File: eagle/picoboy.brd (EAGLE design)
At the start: 72 x 121.7 mm, 10 parts, among them U1 RETROESP32_LM4875

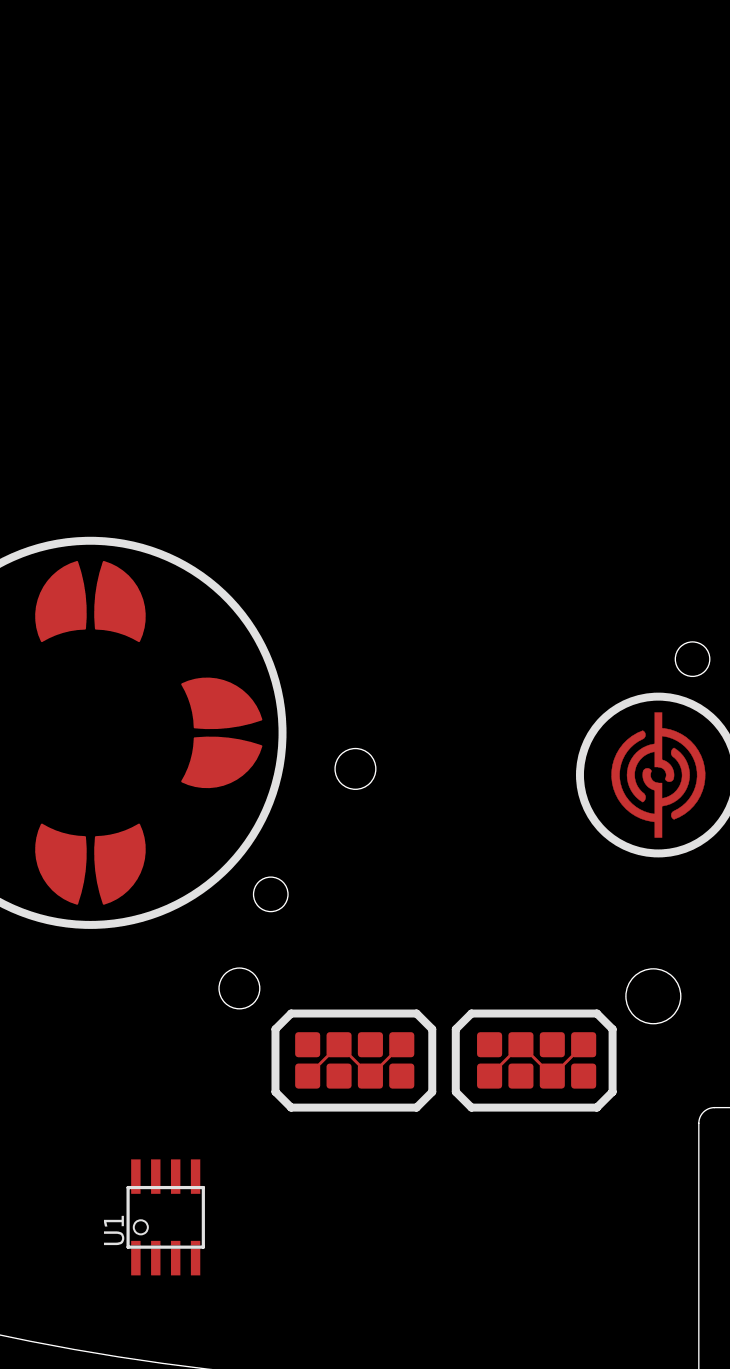
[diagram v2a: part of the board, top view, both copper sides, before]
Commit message: Added devices to library
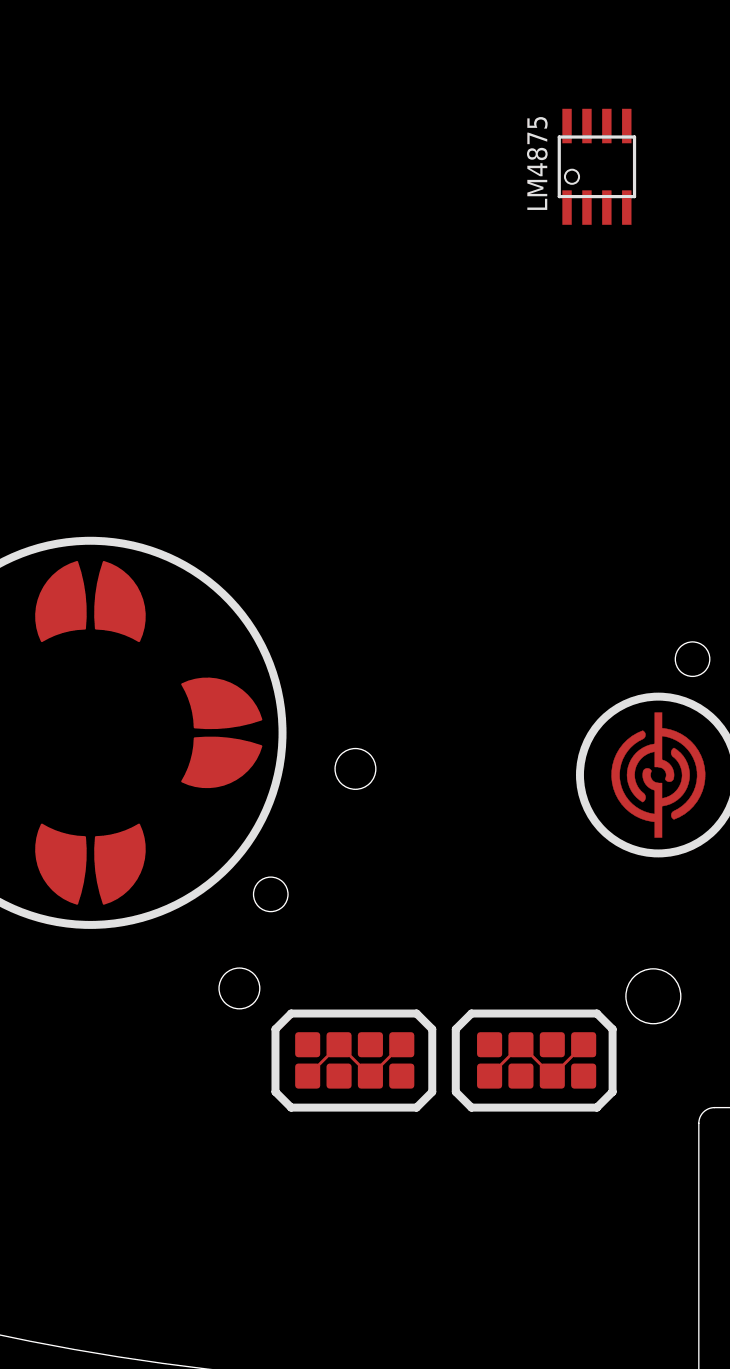
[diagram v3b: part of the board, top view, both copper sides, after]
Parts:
- removed U1: RETROESP32_LM4875, GabozeLite:RETROESP32_SOIC8
- added LM4875: PICOBOY_LM4875, picoboy:PICOBOY_LM4875
- A, B: value RETROESP32_CONDUCTIVE_BUTTONCONDUCTIVE_BUTTON_THICK -> PICOBOY_CONDUCTIVE_BUTTONCONDUCTIVE_BUTTON_THICK; device GabozeLite:RETROESP32_CONDUCTIVE_BUTTON_THICK -> picoboy:PICOBOY_CONDUCTIVE_BUTTON_THICK
- DOWN, LEFT, RIGHT, UP: value RETROESP32_CONDUCTIVE_BUTTONCONDUCTIVE_BUTTON_DIRECTIONAL_THICK -> PICOBOY_CONDUCTIVE_BUTTONCONDUCTIVE_BUTTON_DIRECTIONAL_THICK; device GabozeLite:RETROESP32_CONDUCTIVE_BUTTON_DIRECTIONAL_THICK -> picoboy:PICOBOY_CONDUCTIVE_BUTTON_DIRECTIONAL_THICK
- SELECT, START: value RETROESP32_CONDUCTIVE_BUTTON_STARTSELECTCONDUCTIVE_BUTTON_THICK_STARTSELECT -> PICOBOY_CONDUCTIVE_BUTTON_STARTSELECTCONDUCTIVE_BUTTON_THICK_STARTSELECT; device GabozeLite:RETROESP32_CONDUCTIVE_BUTTON_THICK_STARTSELECT -> picoboy:PICOBOY_CONDUCTIVE_BUTTON_THICK_STARTSELECT
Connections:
- net GND: now also LM4875.6; no longer U1.6
- net VDD: now also LM4875.1; no longer U1.1
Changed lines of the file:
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@@
 </autorouter>
 <elements>
-<element name="UP" library="GabozeLite" package="RETROESP32_CONDUCTIVE_BUTTON_DIRECTIONAL_THICK" value="RETROESP32_CONDUCTIVE_BUTTONCONDUCTIVE_BUTTON_DIRECTIONAL_THICK" x="12.2" y="44.4" smashed="yes" rot="R270"/>
-<element name="RIGHT" library="GabozeLite" package="RETROESP32_CONDUCTIVE_BUTTON_DIRECTIONAL_THICK" value="RETROESP32_CONDUCTIVE_BUTTONCONDUCTIVE_BUTTON_DIRECTIONAL_THICK" x="19.7" y="36.9" smashed="yes" rot="R180"/>
-<element name="DOWN" library="GabozeLite" package="RETROESP32_CONDUCTIVE_BUTTON_DIRECTIONAL_THICK" value="RETROESP32_CONDUCTIVE_BUTTONCONDUCTIVE_BUTTON_DIRECTIONAL_THICK" x="12.2" y="29.4" smashed="yes" rot="R90"/>
-<element name="LEFT" library="GabozeLite" package="RETROESP32_CONDUCTIVE_BUTTON_DIRECTIONAL_THICK" value="RETROESP32_CONDUCTIVE_BUTTONCONDUCTIVE_BUTTON_DIRECTIONAL_THICK" x="4.7" y="36.9" smashed="yes"/>
-<element name="B" library="GabozeLite" package="RETROESP32_CONDUCTIVE_BUTTON_THICK" value="RETROESP32_CONDUCTIVE_BUTTONCONDUCTIVE_BUTTON_THICK" x="48.42" y="34.21" smashed="yes" rot="R180"/>
-<element name="A" library="GabozeLite" package="RETROESP32_CONDUCTIVE_BUTTON_THICK" value="RETROESP32_CONDUCTIVE_BUTTONCONDUCTIVE_BUTTON_THICK" x="62.47" y="38.7" smashed="yes" rot="R180"/>
-<element name="SELECT" library="GabozeLite" package="RETROESP32_CONDUCTIVE_BUTTON_THICK_STARTSELECT" value="RETROESP32_CONDUCTIVE_BUTTON_STARTSELECTCONDUCTIVE_BUTTON_THICK_STARTSELECT" x="29.055" y="16.01" smashed="yes"/>
-<element name="START" library="GabozeLite" package="RETROESP32_CONDUCTIVE_BUTTON_THICK_STARTSELECT" value="RETROESP32_CONDUCTIVE_BUTTON_STARTSELECTCONDUCTIVE_BUTTON_THICK_STARTSELECT" x="40.655" y="16.01" smashed="yes"/>
-<element name="U1" library="GabozeLite" package="RETROESP32_SOIC8" value="RETROESP32_LM4875" x="17" y="6" smashed="yes">
-<attribute name="NAME" x="14.333" y="4.095" size="1.27" layer="25" rot="R90"/>
-<attribute name="VALUE" x="20.937" y="4.095" size="1.27" layer="27" rot="R90"/>
+<element name="UP" library="picoboy" package="PICOBOY_CONDUCTIVE_BUTTON_DIRECTIONAL_THICK" value="PICOBOY_CONDUCTIVE_BUTTONCONDUCTIVE_BUTTON_DIRECTIONAL_THICK" x="12.2" y="44.4" smashed="yes" rot="R270"/>
+<element name="RIGHT" library="picoboy" package="PICOBOY_CONDUCTIVE_BUTTON_DIRECTIONAL_THICK" value="PICOBOY_CONDUCTIVE_BUTTONCONDUCTIVE_BUTTON_DIRECTIONAL_THICK" x="19.7" y="36.9" smashed="yes" rot="R180"/>
+<element name="DOWN" library="picoboy" package="PICOBOY_CONDUCTIVE_BUTTON_DIRECTIONAL_THICK" value="PICOBOY_CONDUCTIVE_BUTTONCONDUCTIVE_BUTTON_DIRECTIONAL_THICK" x="12.2" y="29.4" smashed="yes" rot="R90"/>
+<element name="LEFT" library="picoboy" package="PICOBOY_CONDUCTIVE_BUTTON_DIRECTIONAL_THICK" value="PICOBOY_CONDUCTIVE_BUTTONCONDUCTIVE_BUTTON_DIRECTIONAL_THICK" x="4.7" y="36.9" smashed="yes"/>
+<element name="B" library="picoboy" package="PICOBOY_CONDUCTIVE_BUTTON_THICK" value="PICOBOY_CONDUCTIVE_BUTTONCONDUCTIVE_BUTTON_THICK" x="48.42" y="34.21" smashed="yes" rot="R180"/>
+<element name="A" library="picoboy" package="PICOBOY_CONDUCTIVE_BUTTON_THICK" value="PICOBOY_CONDUCTIVE_BUTTONCONDUCTIVE_BUTTON_THICK" x="62.47" y="38.7" smashed="yes" rot="R180"/>
+<element name="SELECT" library="picoboy" package="PICOBOY_CONDUCTIVE_BUTTON_THICK_STARTSELECT" value="PICOBOY_CONDUCTIVE_BUTTON_STARTSELECTCONDUCTIVE_BUTTON_THICK_STARTSELECT" x="29.055" y="16.01" smashed="yes"/>
+<element name="START" library="picoboy" package="PICOBOY_CONDUCTIVE_BUTTON_THICK_STARTSELECT" value="PICOBOY_CONDUCTIVE_BUTTON_STARTSELECTCONDUCTIVE_BUTTON_THICK_STARTSELECT" x="40.655" y="16.01" smashed="yes"/>
+<element name="LM4875" library="picoboy" package="PICOBOY_LM4875" value="PICOBOY_LM4875" x="44.5" y="73" smashed="yes">
+<attribute name="NAME" x="41.333" y="70.095" size="1.27" layer="25" rot="R90"/>
 </element>
 <element name="U$1" library="picoboy" package="PICOBOY_GBC_BOARD_OUTLINE" value="" x="0" y="0" smashed="yes"/>
@@
 <signals>
 <signal name="GND">
-<contactref element="U1" pad="6"/>
+<contactref element="LM4875" pad="6"/>
 </signal>
 <signal name="VDD">
-<contactref element="U1" pad="1"/>
+<contactref element="LM4875" pad="1"/>
 </signal>
 </signals>

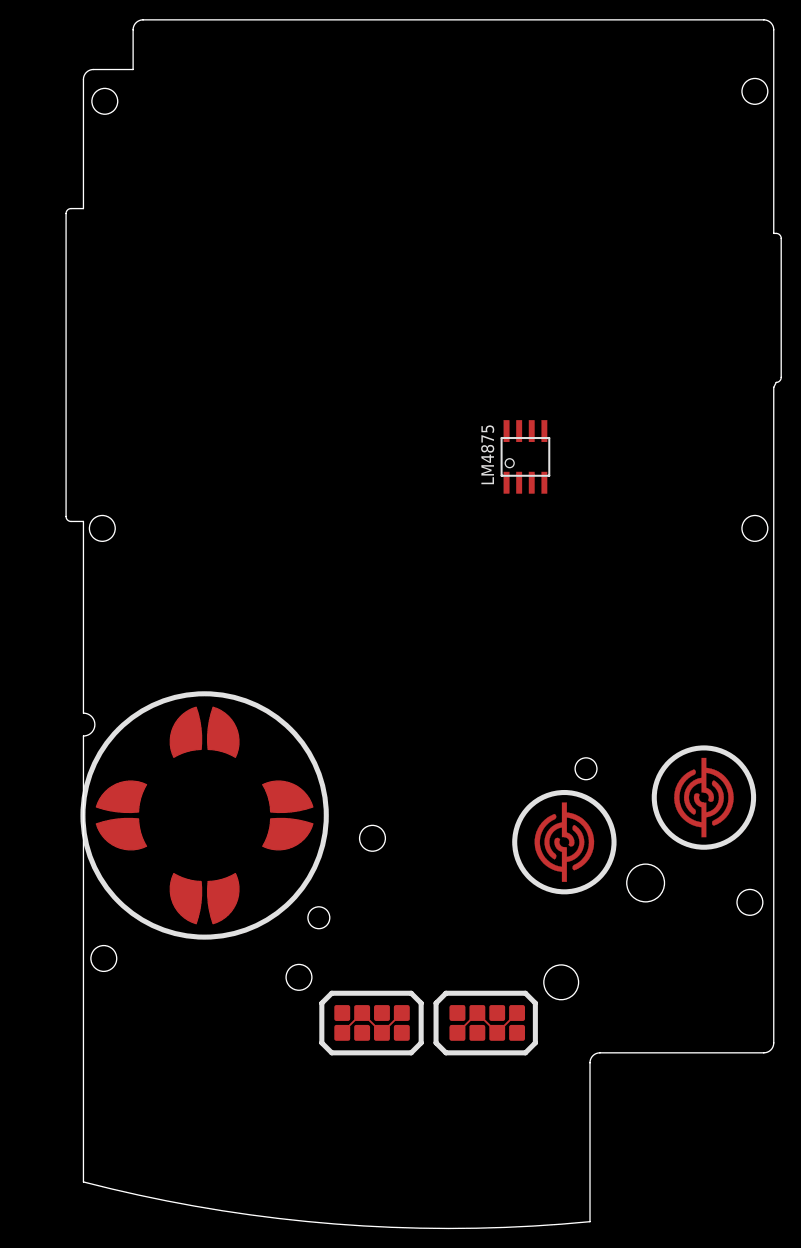
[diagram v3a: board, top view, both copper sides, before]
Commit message: Start amplifier schematics
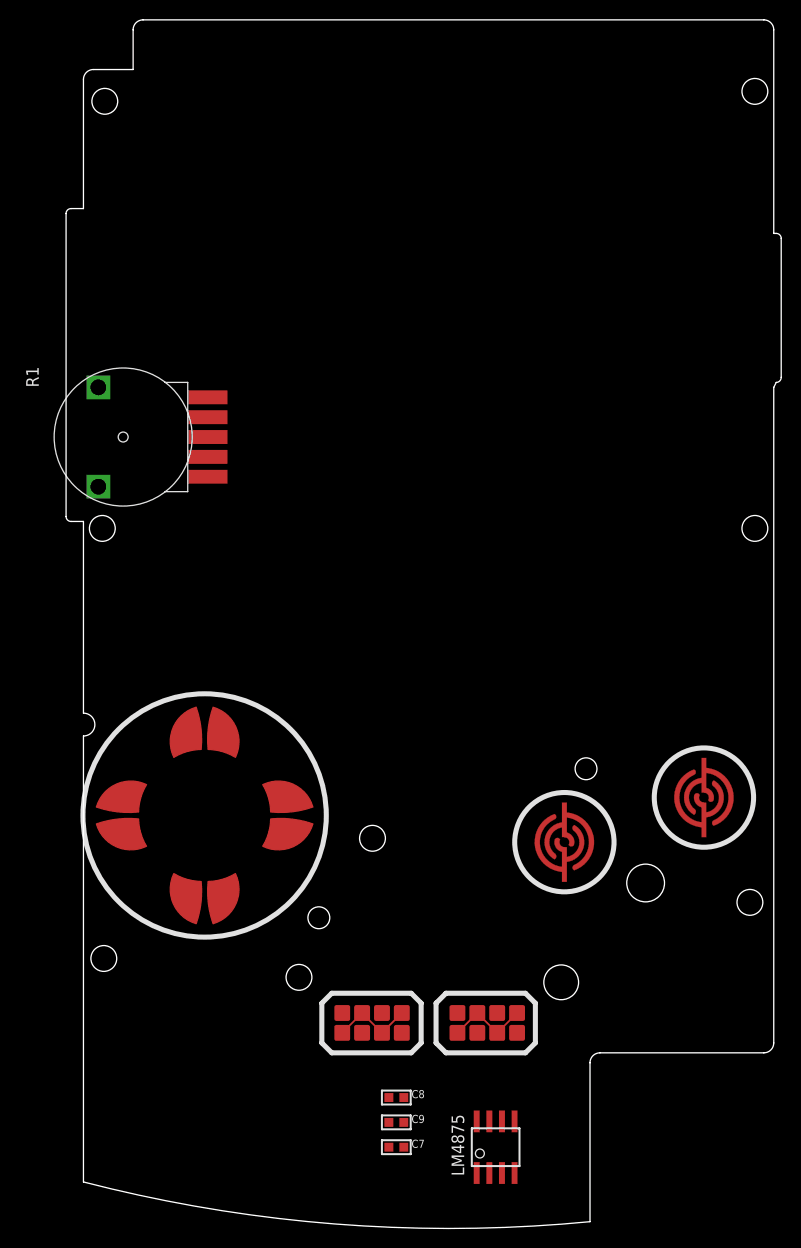
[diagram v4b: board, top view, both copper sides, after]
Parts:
- added C7: 0.22uF, picoboy:PICOBOY_CAPACITOR_0603-MINI
- added C8, C9: 1uF, picoboy:PICOBOY_CAPACITOR_0603-MINI
- added R1: (no value), picoboy:PICOBOY_VOLUME_WHEEL
- moved LM4875 69.6 mm to (41.5, 3.50)
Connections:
- removed net VDD: LM4875.1
- new net 3V3: R1.5
- new net AUDIO: C7.1
- new net N$1: C8.1, LM4875.7
- new net N$2: C9.1, LM4875.1
- new net N$3: C7.2, LM4875.2
- new net N$4: LM4875.4, R1.3
- net GND: now also C8.2, C9.2, R1.1
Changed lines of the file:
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@@
 <element name="SELECT" library="picoboy" package="PICOBOY_CONDUCTIVE_BUTTON_THICK_STARTSELECT" value="PICOBOY_CONDUCTIVE_BUTTON_STARTSELECTCONDUCTIVE_BUTTON_THICK_STARTSELECT" x="29.055" y="16.01" smashed="yes"/>
 <element name="START" library="picoboy" package="PICOBOY_CONDUCTIVE_BUTTON_THICK_STARTSELECT" value="PICOBOY_CONDUCTIVE_BUTTON_STARTSELECTCONDUCTIVE_BUTTON_THICK_STARTSELECT" x="40.655" y="16.01" smashed="yes"/>
-<element name="LM4875" library="picoboy" package="PICOBOY_LM4875" value="PICOBOY_LM4875" x="44.5" y="73" smashed="yes">
-<attribute name="NAME" x="41.333" y="70.095" size="1.27" layer="25" rot="R90"/>
+<element name="LM4875" library="picoboy" package="PICOBOY_LM4875" value="PICOBOY_LM4875" x="41.5" y="3.5" smashed="yes">
+<attribute name="NAME" x="38.333" y="0.595" size="1.27" layer="25" rot="R90"/>
 </element>
 <element name="U$1" library="picoboy" package="PICOBOY_GBC_BOARD_OUTLINE" value="" x="0" y="0" smashed="yes"/>
+<element name="C8" library="picoboy" package="PICOBOY_CAPACITOR_0603-MINI" value="1uF" x="31.5" y="8.5" smashed="yes">
+<attribute name="NAME" x="33.024" y="8.4365" size="0.8128" layer="25" ratio="18"/>
+<attribute name="NAME" x="33.024" y="8.4365" size="0.8128" layer="25" ratio="18"/>
+<attribute name="VALUE" x="33.024" y="7.865" size="0.4064" layer="27" ratio="10"/>
+<attribute name="VALUE" x="33.024" y="7.865" size="0.4064" layer="27" ratio="10"/>
+</element>
+<element name="C9" library="picoboy" package="PICOBOY_CAPACITOR_0603-MINI" value="1uF" x="31.5" y="6" smashed="yes">
+<attribute name="NAME" x="33.024" y="5.9365" size="0.8128" layer="25" ratio="18"/>
+<attribute name="NAME" x="33.024" y="5.9365" size="0.8128" layer="25" ratio="18"/>
+<attribute name="VALUE" x="33.024" y="5.365" size="0.4064" layer="27" ratio="10"/>
+<attribute name="VALUE" x="33.024" y="5.365" size="0.4064" layer="27" ratio="10"/>
+</element>
+<element name="C7" library="picoboy" package="PICOBOY_CAPACITOR_0603-MINI" value="0.22uF" x="31.5" y="3.5" smashed="yes">
+<attribute name="NAME" x="33.024" y="3.4365" size="0.8128" layer="25" ratio="18"/>
+<attribute name="NAME" x="33.024" y="3.4365" size="0.8128" layer="25" ratio="18"/>
+<attribute name="VALUE" x="33.024" y="2.865" size="0.4064" layer="27" ratio="10"/>
+<attribute name="VALUE" x="33.024" y="2.865" size="0.4064" layer="27" ratio="10"/>
+</element>
+<element name="R1" library="picoboy" package="PICOBOY_VOLUME_WHEEL" value="" x="10.5" y="75" smashed="yes" rot="R90">
+<attribute name="NAME" x="-4.5" y="80" size="1.27" layer="25" rot="R90"/>
+<attribute name="VALUE" x="-2.5" y="80" size="1.27" layer="27" rot="R90"/>
+</element>
 </elements>
 <signals>
 <signal name="GND">
 <contactref element="LM4875" pad="6"/>
+<contactref element="C8" pad="2"/>
+<contactref element="C9" pad="2"/>
+<contactref element="R1" pad="1"/>
+<wire x1="32.25" y1="8.5" x2="12.5" y2="71" width="0" layer="19" extent="1-1"/>
+<wire x1="32.25" y1="6" x2="32.25" y2="8.5" width="0" layer="19" extent="1-1"/>
+<wire x1="42.135" y1="6.1" x2="32.25" y2="6" width="0" layer="19" extent="1-1"/>
 </signal>
-<signal name="VDD">
+<signal name="N$1">
+<contactref element="LM4875" pad="7"/>
+<contactref element="C8" pad="1"/>
+<wire x1="30.75" y1="8.5" x2="40.865" y2="6.1" width="0" layer="19" extent="1-1"/>
+</signal>
+<signal name="N$2">
 <contactref element="LM4875" pad="1"/>
+<contactref element="C9" pad="1"/>
+<wire x1="30.75" y1="6" x2="39.595" y2="0.9" width="0" layer="19" extent="1-1"/>
+</signal>
+<signal name="N$3">
+<contactref element="LM4875" pad="2"/>
+<contactref element="C7" pad="2"/>
+<wire x1="32.25" y1="3.5" x2="40.865" y2="0.9" width="0" layer="19" extent="1-1"/>
+</signal>
+<signal name="N$4">
+<contactref element="R1" pad="3"/>
+<contactref element="LM4875" pad="4"/>
+<wire x1="43.405" y1="0.9" x2="12.5" y2="75" width="0" layer="19" extent="1-1"/>
+</signal>
+<signal name="3V3">
+<contactref element="R1" pad="5"/>
+</signal>
+<signal name="AUDIO">
+<contactref element="C7" pad="1"/>
 </signal>
 </signals>
